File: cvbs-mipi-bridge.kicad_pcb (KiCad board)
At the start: 4 copper layers, 55 x 59.7 mm, 105 parts, among them IC1 ADV7280BCPZ-M, IC2 TLV70018, IC4 SN74AUP1G17DCKR, IC5 SN74AUP1G17DCKR, J1 WE_68715014522, J2 61300211121, J7 61300211121, Q1 BSS138APW, Q2 BSS138APW, Q3 BSS138APW, Q4 BSS138APW, Y1 ABM8G-28.63636MHZ-18-D2Y-T

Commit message: Cleanup
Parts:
- AIN1, AIN2, AIN3, AIN4: footprint antmicro-cvbs-mipi-bridge-footprints:PJRAN1X1U01X -> cvbs-mipi-bridge-footprints:PJRAN1X1U01X
- C1, C10, C11, C13, C14, C15, C16, C17, C18, C19, C2, C20, C21, C22, C23, C24, C26, C27, C28, C3, C4, C5, C6, C7, C8, C9: footprint antmicro-cvbs-mipi-bridge-footprints:0402-cap -> cvbs-mipi-bridge-footprints:0402-cap
- C12: footprint antmicro-cvbs-mipi-bridge-footprints:0603-cap -> cvbs-mipi-bridge-footprints:0603-cap
- D1, D2, D3, D4: footprint antmicro-cvbs-mipi-bridge-footprints:SOT-23-3 -> cvbs-mipi-bridge-footprints:SOT-23-3
- D5, D6, D7, D8: footprint antmicro-cvbs-mipi-bridge-footprints:LED_0603 -> cvbs-mipi-bridge-footprints:LED_0603
- FB1, FB3, FB4, FB5: footprint antmicro-cvbs-mipi-bridge-footprints:0805-res -> cvbs-mipi-bridge-footprints:0805-res
- IC1: footprint antmicro-cvbs-mipi-bridge-footprints:LFCSP-32-1EP-5x5mm -> cvbs-mipi-bridge-footprints:LFCSP-32-1EP-5x5mm
- IC2: footprint antmicro-cvbs-mipi-bridge-footprints:SC-70-5 -> cvbs-mipi-bridge-footprints:SC-70-5
- IC4, IC5: footprint antmicro-cvbs-mipi-bridge-footprints:SOT-753 -> cvbs-mipi-bridge-footprints:SOT-753
- J1: footprint antmicro-cvbs-mipi-bridge-footprints:WE_68715014522 -> cvbs-mipi-bridge-footprints:WE_68715014522
- J2, J7: footprint antmicro-cvbs-mipi-bridge-footprints:PinHeader_1x2_P2.54_Drill0.9mm -> cvbs-mipi-bridge-footprints:PinHeader_1x2_P2.54_Drill0.9mm
- MP1, MP2, MP3, MP4: footprint antmicro-cvbs-mipi-bridge-footprints:9774030243R -> cvbs-mipi-bridge-footprints:9774030243R
- N1: footprint antmicro-cvbs-mipi-bridge-footprints:antmicro-logo_scaled_20mm -> cvbs-mipi-bridge-footprints:antmicro-logo_scaled_20mm
- N2: footprint antmicro-cvbs-mipi-bridge-footprints:oshw-logo -> cvbs-mipi-bridge-footprints:oshw-logo
- Q1, Q2, Q3, Q4: footprint antmicro-cvbs-mipi-bridge-footprints:SC70-3 -> cvbs-mipi-bridge-footprints:SC70-3
- R1, R10, R4, R8: footprint antmicro-cvbs-mipi-bridge-footprints:0603-res -> cvbs-mipi-bridge-footprints:0603-res
- R11, R12, R13, R14, R15, R16, R17, R18, R19, R2, R20, R21, R22, R23, R24, R25, R26, R27, R28, R29, R3, R30, R31, R5, R6, R7, R9: footprint antmicro-cvbs-mipi-bridge-footprints:0402-res -> cvbs-mipi-bridge-footprints:0402-res
- S1: footprint antmicro-cvbs-mipi-bridge-footprints:SW_SPST_4.2x2.8 -> cvbs-mipi-bridge-footprints:SW_SPST_4.2x2.8
- TP1, TP10, TP11, TP12, TP13, TP2, TP3, TP5, TP6, TP7, TP8, TP9: footprint antmicro-cvbs-mipi-bridge-footprints:TP-R-1.5 -> cvbs-mipi-bridge-footprints:TP-R-1.5
- Y1: footprint antmicro-cvbs-mipi-bridge-footprints:KX-7 -> cvbs-mipi-bridge-footprints:KX-7

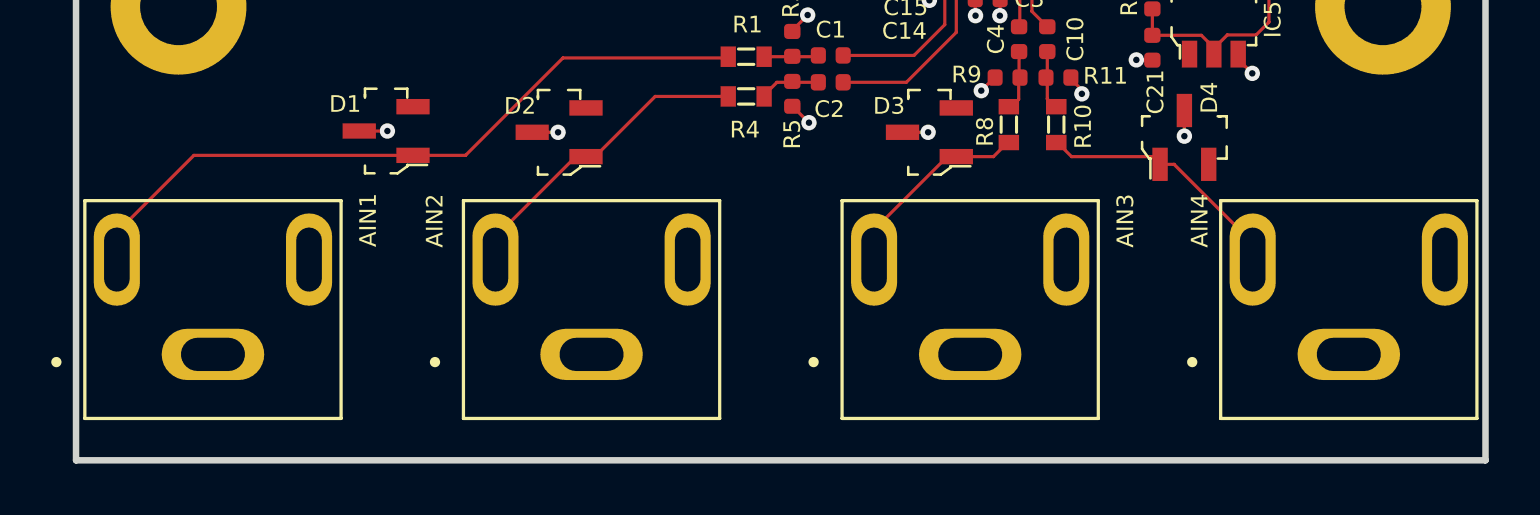
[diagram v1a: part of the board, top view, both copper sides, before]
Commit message: Replace RCA connectors
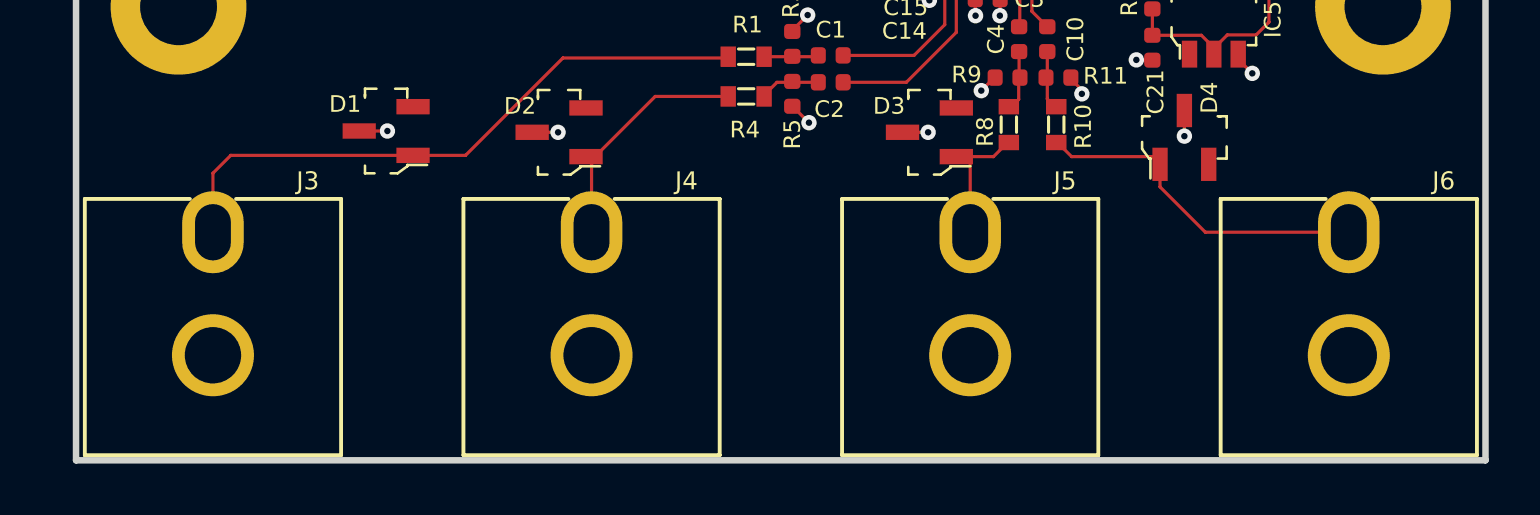
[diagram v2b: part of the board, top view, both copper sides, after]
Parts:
- removed AIN1, AIN2, AIN3, AIN4: PJRAN1X1U01X, cvbs-mipi-bridge-footprints:PJRAN1X1U01X
- added J3: KLPX-0848A-2-Y, cvbs-mipi-bridge-footprints:KLPX-0848A-2-Y, F.Cu at (117.0, 115.5)
- added J4: KLPX-0848A-2-Y, cvbs-mipi-bridge-footprints:KLPX-0848A-2-Y, F.Cu at (131.8, 115.5)
- added J5: KLPX-0848A-2-Y, cvbs-mipi-bridge-footprints:KLPX-0848A-2-Y, F.Cu at (146.6, 115.5)
- added J6: KLPX-0848A-2-Y, cvbs-mipi-bridge-footprints:KLPX-0848A-2-Y, F.Cu at (161.4, 115.5)
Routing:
- net /AIN4_ESD: track 9.24 -> 13.3 mm
- net /AIN1_ESD: track 26.6 -> 24.2 mm
- net /AIN2_ESD: track 10.6 -> 9.21 mm
- net /AIN3_ESD: track 6.27 -> 5.03 mm

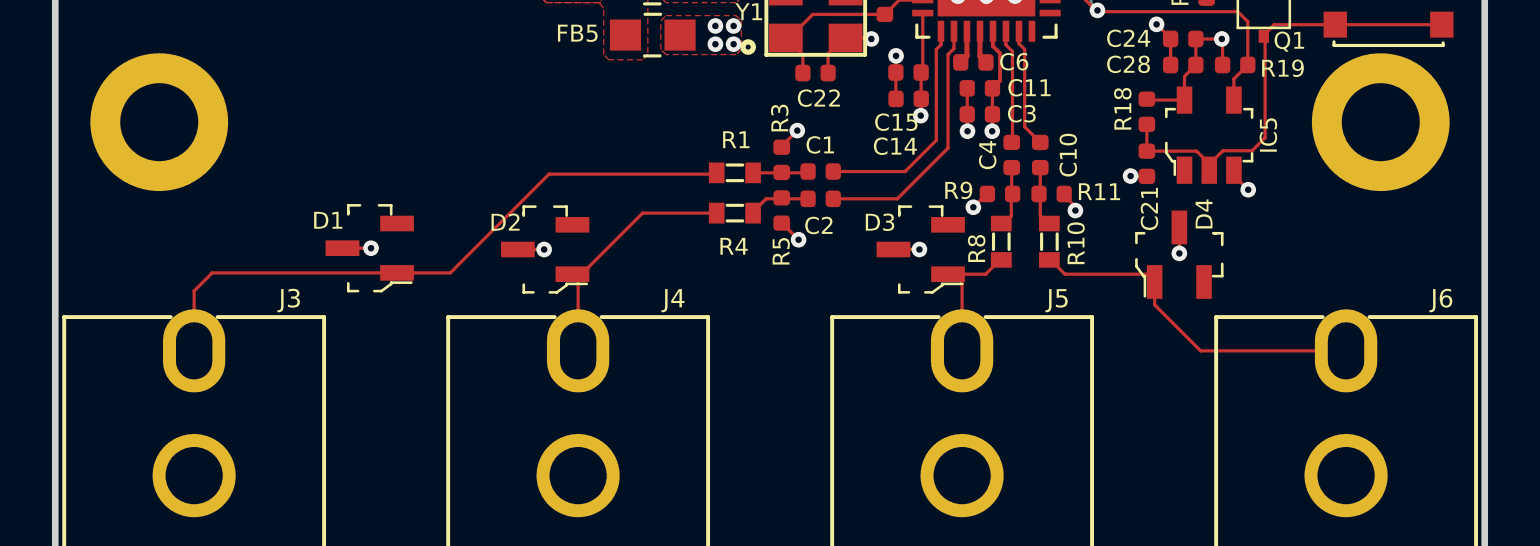
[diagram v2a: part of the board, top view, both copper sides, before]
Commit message: Replace TVS diodes
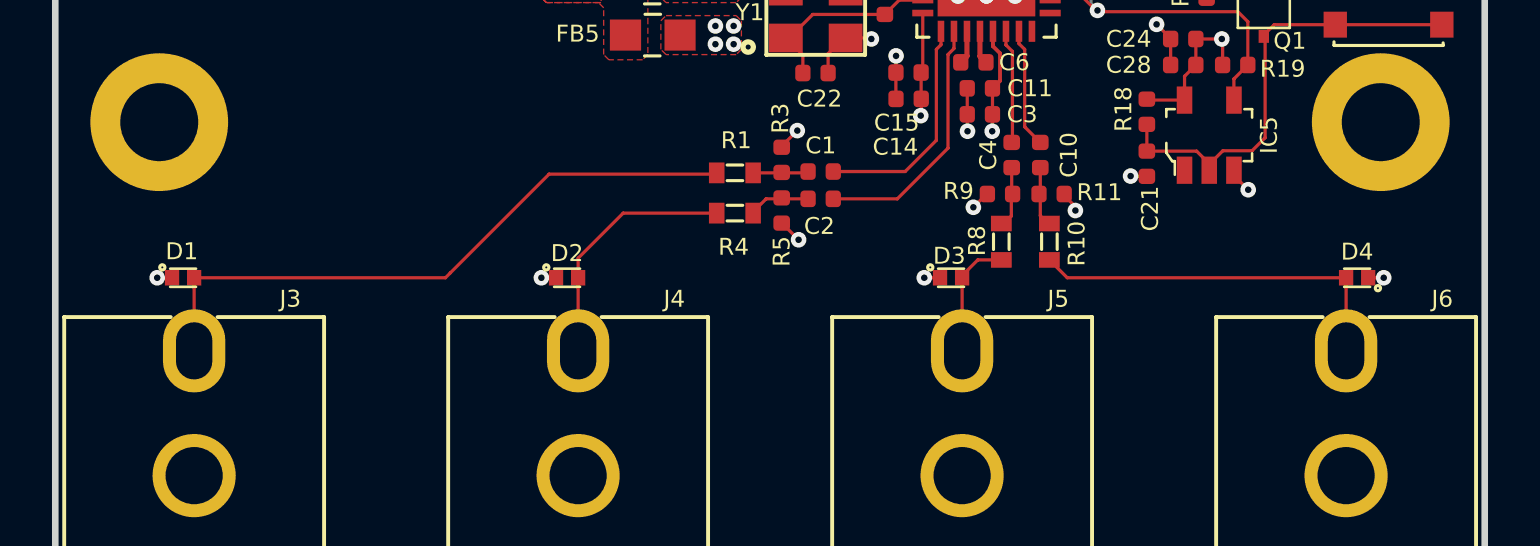
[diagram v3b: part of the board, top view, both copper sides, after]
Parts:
- D1, D2, D3, D4: value PESD1CAN_215 -> UCLAMP2501T.TCT; footprint cvbs-mipi-bridge-footprints:SOT-23-3 -> cvbs-mipi-bridge-footprints:SLP1006P2T
- moved D1 7.27 mm to (116.6, 104.0), turned to 0 degrees
- moved D4 6.90 mm to (161.8, 104.0), turned to 180 degrees
- moved D3 1.59 mm to (146.2, 104.0), turned to 0 degrees
- moved D2 1.38 mm to (131.4, 104.0), turned to 0 degrees
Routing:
- net GND: track 55.0 -> 53.3 mm
- net /AIN4_ESD: track 13.3 -> 14.5 mm

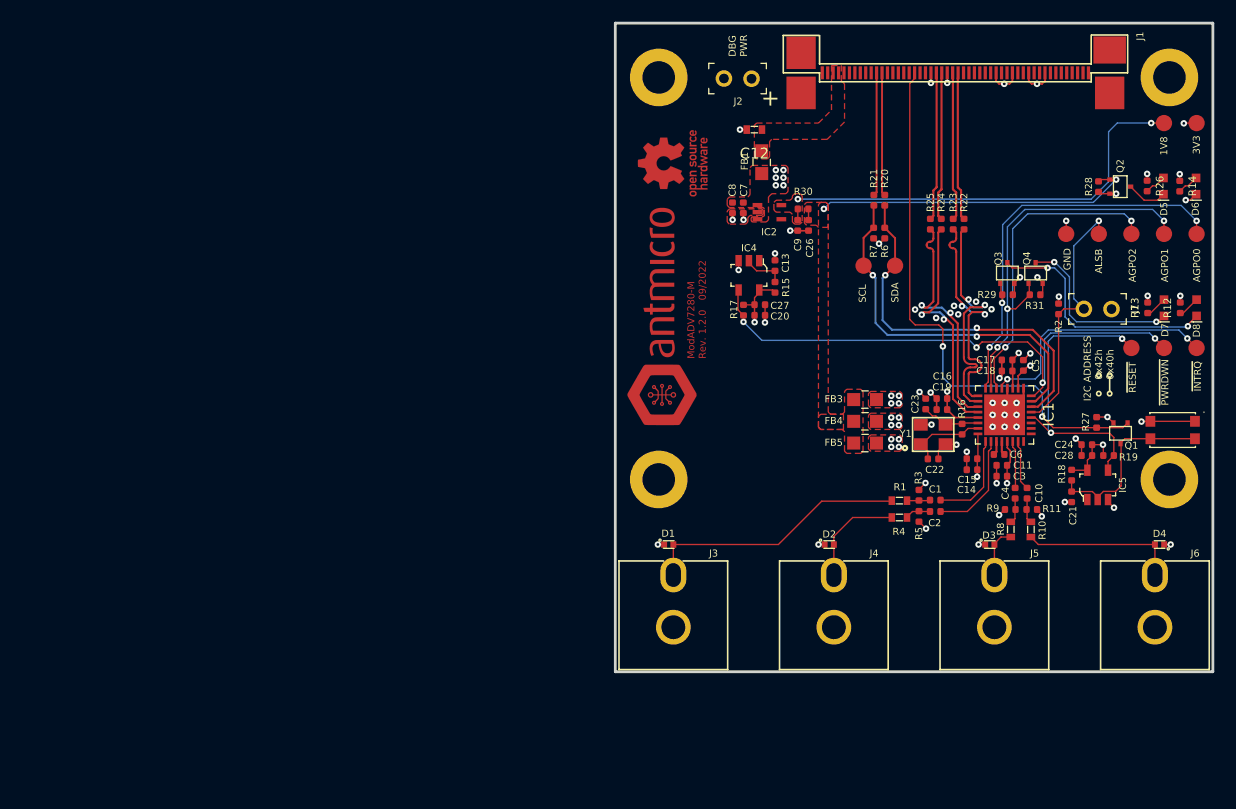
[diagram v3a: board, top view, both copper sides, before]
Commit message: Rearrange connectors (WiP)
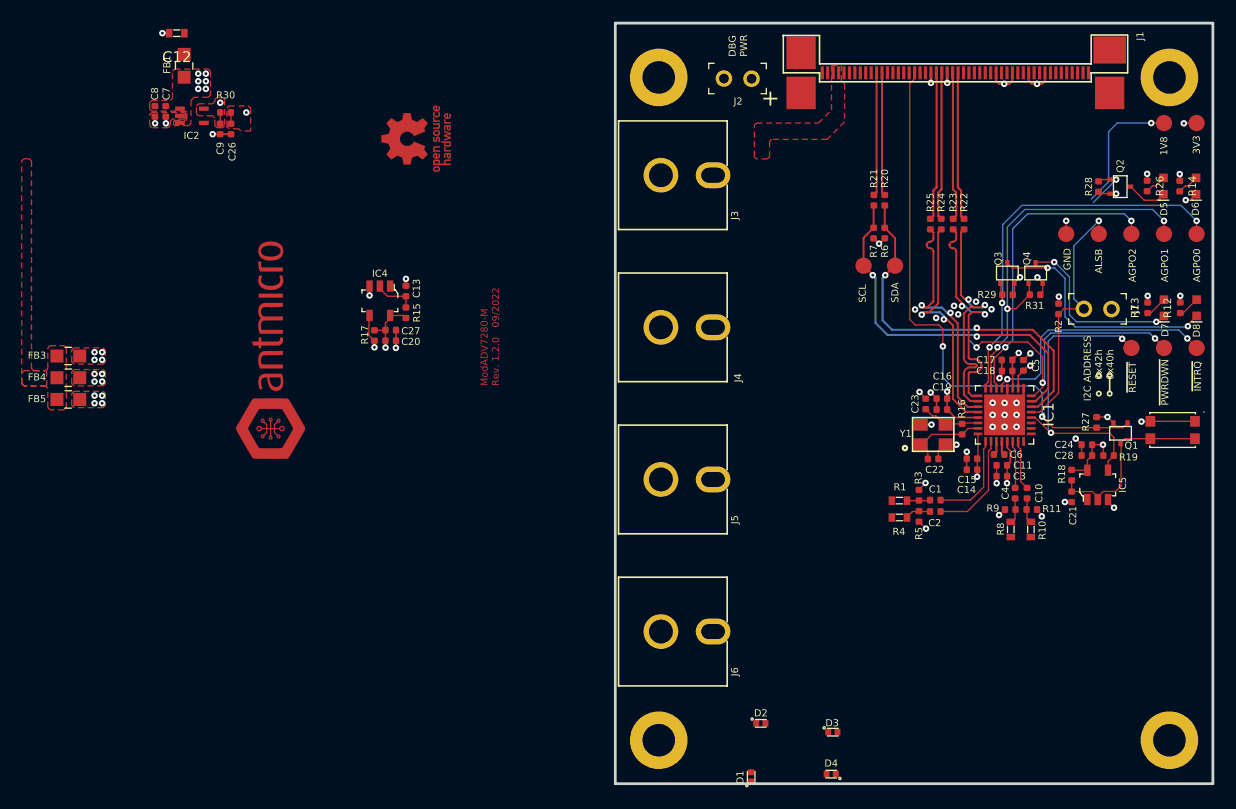
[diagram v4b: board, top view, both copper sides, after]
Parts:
- moved FB3 73.4 mm to (61.4, 86.6)
- moved FB4 73.4 mm to (61.4, 88.6)
- moved FB5 73.4 mm to (61.4, 90.6)
- moved C26 53.9 mm to (76.3, 65.7)
- moved C9 53.9 mm to (75.3, 65.7)
- moved R30 53.9 mm to (75.8, 64.2)
- moved C12 53.9 mm to (71.3, 56.9)
- moved C7 53.9 mm to (70.3, 64.1)
- moved C8 53.9 mm to (69.3, 64.1)
- moved IC2 53.9 mm to (72.7, 64.5)
- moved FB1 53.9 mm to (72.0, 59.9)
- moved J6 49.5 mm to (112.0, 112.0), turned to 0 degrees
- moved J3 45.8 mm to (112.0, 70.0), turned to 0 degrees
- moved J5 38.8 mm to (112.0, 98.0), turned to 0 degrees
- moved J4 37.2 mm to (112.0, 84.0), turned to 0 degrees
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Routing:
- net Net-(C9-Pad1): track 40.3 -> 13.3 mm
- net 1V8_SYS: track 30.5 -> 5.44 mm
- net /AIN1_ESD: track 24.5 -> 0.00 mm
- net /PWRDWN: track 52.1 -> 30.6 mm
- net /AIN4_ESD: track 14.5 -> 0.00 mm
- net /AIN2_ESD: track 9.62 -> 0.00 mm
- net /AIN3_ESD: track 4.66 -> 0.00 mm
- net GND: track 53.3 -> 50.3 mm, vias 52 -> 48
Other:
- board size 55 x 59.7 mm -> 55 x 70 mm

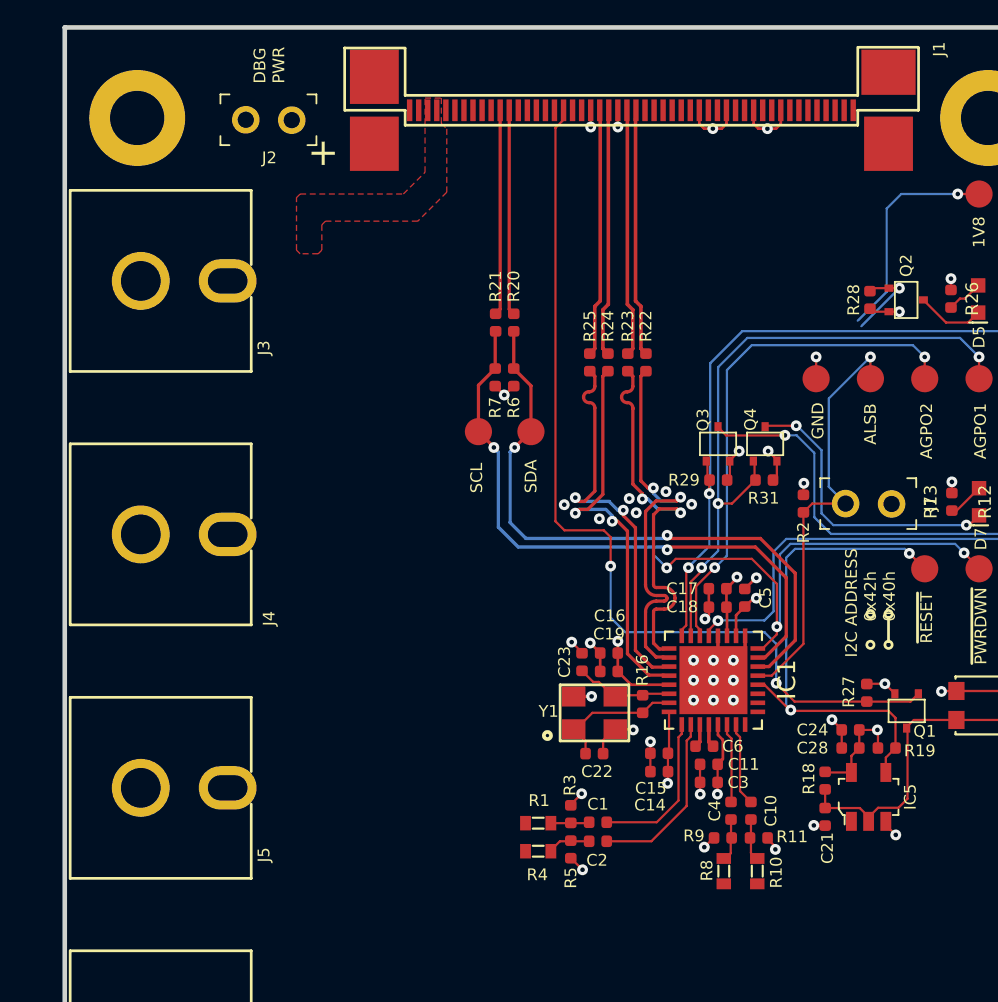
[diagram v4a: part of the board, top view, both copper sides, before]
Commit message: Rearrange components (WiP)
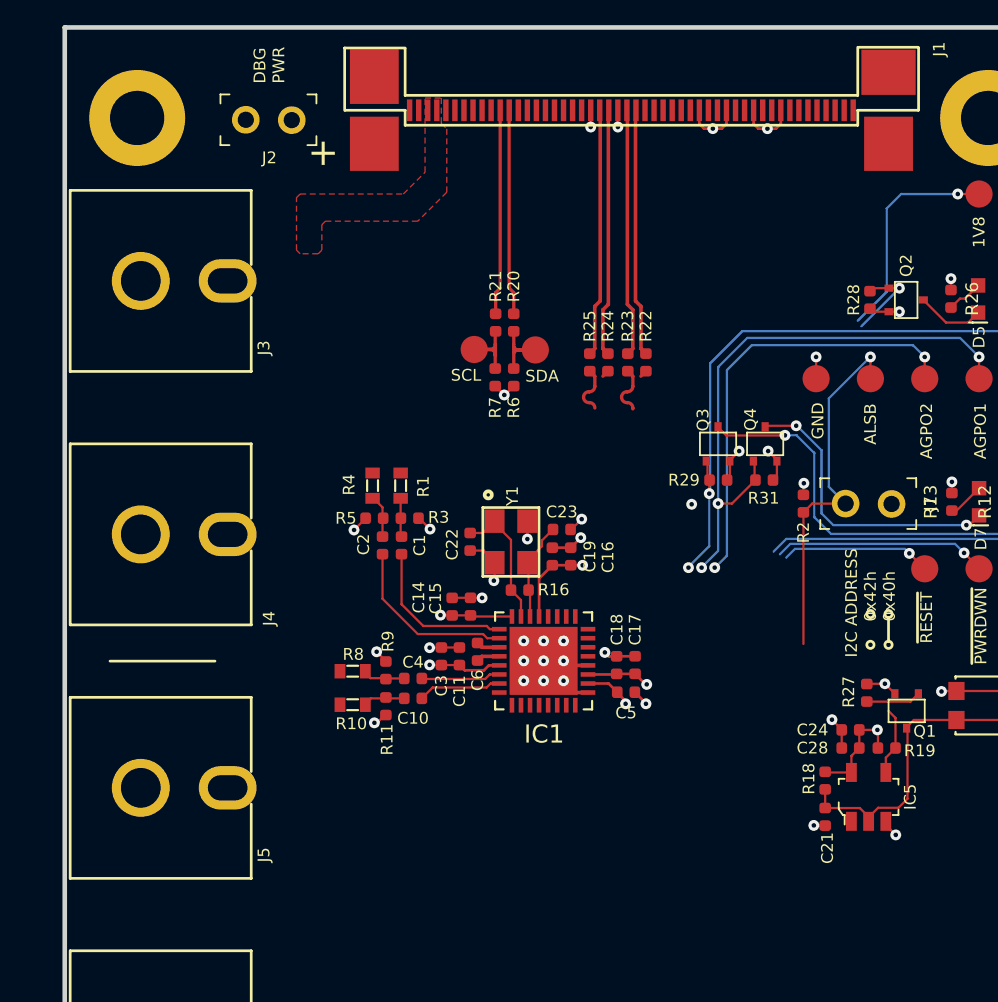
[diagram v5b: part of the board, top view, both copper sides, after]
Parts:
- moved R10 24.2 mm to (127.6, 93.4), turned to 0 degrees
- moved R8 23.3 mm to (127.6, 91.6), turned to 0 degrees
- moved R4 22.2 mm to (128.7, 81.3), turned to -90 degrees
- moved R11 21.8 mm to (129.4, 93.5), turned to 90 degrees
- moved R5 21.3 mm to (128.8, 83.1), turned to 0 degrees
- moved R9 20.8 mm to (129.4, 91.5), turned to -90 degrees
- moved C2 20.2 mm to (129.3, 84.6), turned to -90 degrees
- moved R1 20.1 mm to (130.3, 81.3), turned to -90 degrees
- moved C10 19.7 mm to (130.9, 93.1), turned to 0 degrees
- moved C4 19.0 mm to (130.9, 92.0), turned to 0 degrees
- moved C1 18.7 mm to (130.3, 84.6), turned to -90 degrees
- moved R3 18.6 mm to (130.8, 83.1), turned to 180 degrees
- moved C3 16.3 mm to (132.5, 90.7), turned to -90 degrees
- moved C11 15.0 mm to (133.5, 90.7), turned to 90 degrees
- moved C14 14.6 mm to (133.1, 88.0), turned to -90 degrees
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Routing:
- net /RST_IN: track 50.6 -> 3.03 mm, vias 2 -> 0
- net /SDA: track 34.9 -> 5.08 mm, vias 2 -> 0
- net /SCL: track 34.1 -> 6.01 mm, vias 2 -> 0
- net /CSI_A_CLK_N: track 21.8 -> 0.39 mm, vias 2 -> 0
- net /CSI_A_D0_N: track 21.7 -> 0.39 mm, vias 2 -> 0
- net /CSI_A_CLK_P: track 21.7 -> 2.84 mm, vias 2 -> 0
- net /CSI_A_D0_P: track 21.7 -> 2.89 mm, vias 2 -> 0
- net /RESET: track 28.4 -> 12.1 mm, vias 2 -> 1
- net /PWRDWN: track 30.6 -> 14.9 mm, vias 4 -> 2
- net Net-(IC1-Pad5): track 22.6 -> 15.3 mm, vias 2 -> 1
- net Net-(IC1-Pad6): track 28.4 -> 24.5 mm
- net /AGPO1: track 35.7 -> 31.9 mm
- net /AGPO0: track 37.4 -> 33.7 mm
- net /ALSB: track 23.7 -> 20.4 mm
- net GND: vias 48 -> 43
